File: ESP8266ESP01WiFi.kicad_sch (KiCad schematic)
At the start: 5 parts, among them IC1 TXS0104ED, J1 M20-7830446, U1 ESP-01v090

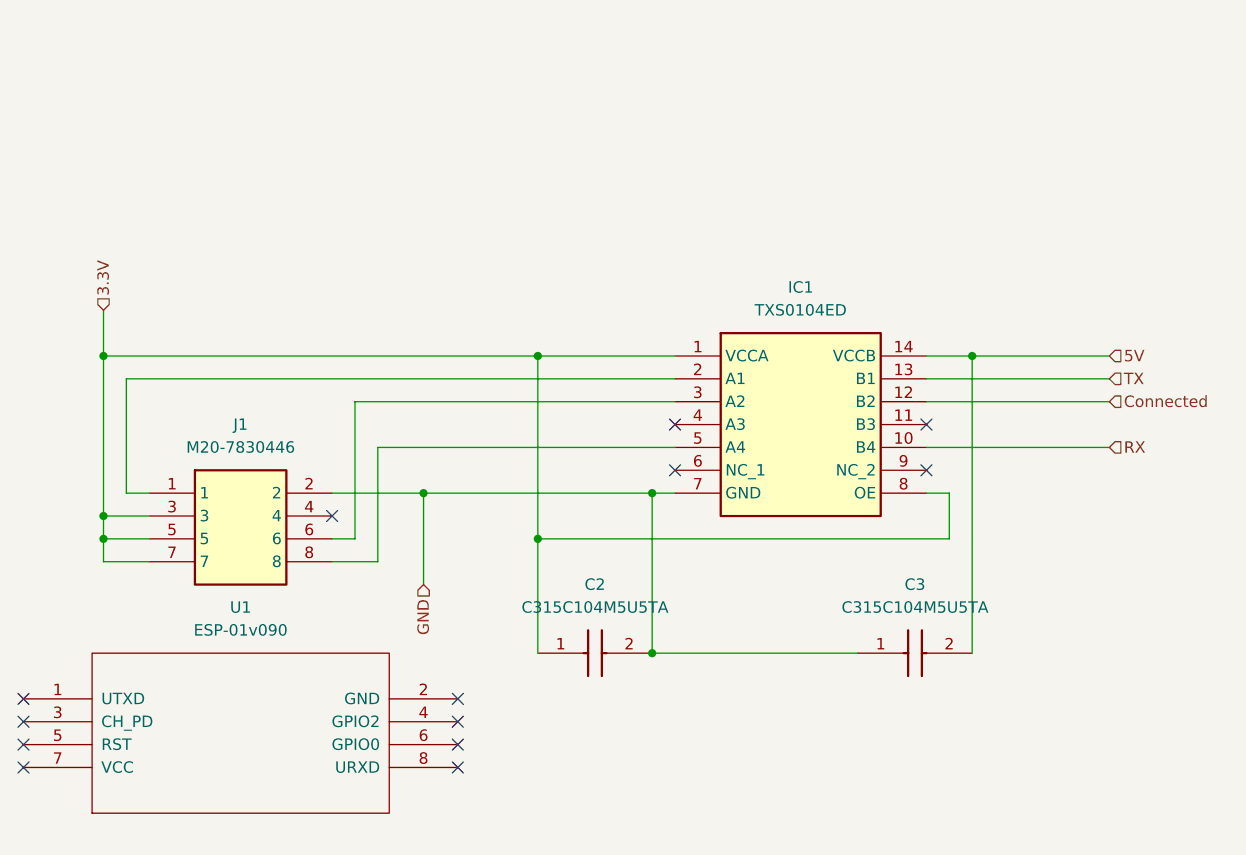
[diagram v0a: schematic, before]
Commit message: Swapped components for those in custom library, updated labelling on PCB.
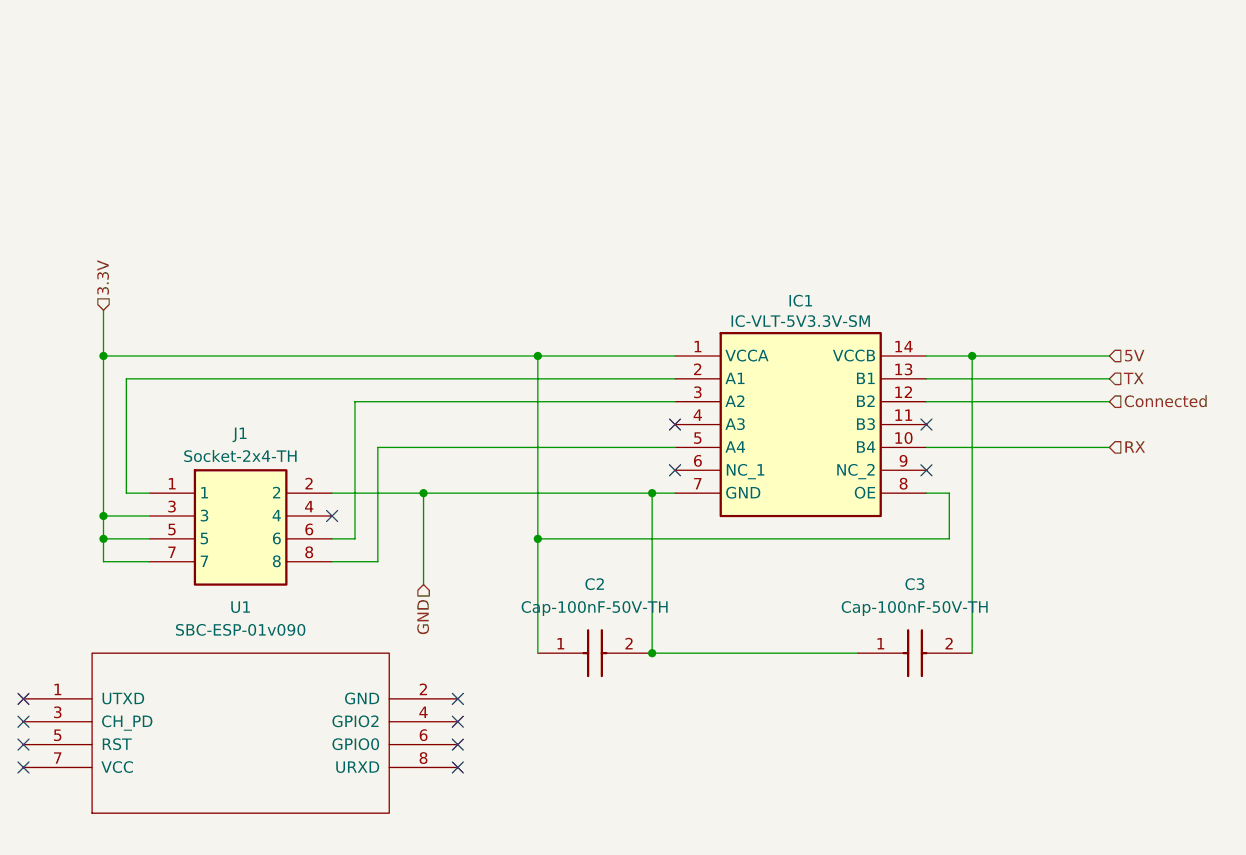
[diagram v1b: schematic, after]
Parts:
- C2, C3: value C315C104M5U5TA -> Cap-100nF-50V-TH; footprint SamacSys_Parts:C315C100J2G5TA -> Custom:80-C315C104M5U; symbol SamacSys_Parts:C315C104M5U5TA -> Custom:Cap-100nF-50V-TH; Supplier (none) -> Mouser; Supplier Part Number (none) -> 80-C315C104M5U; Supplier Price/Stock (none) -> https://www.mouser.co.uk/ProductDetail/KEMET/C315C104M5U5TA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
- IC1: value TXS0104ED -> IC-VLT-5V3.3V-SM; footprint SamacSys_Parts:SOIC127P600X175-14N -> Custom:595-TXS0104ED; symbol SamacSys_Parts:TXS0104ED -> Custom:IC-VLT-5V3.3V-SM; Supplier (none) -> Mouser; Supplier Part Number (none) -> 595-TXS0104ED; Supplier Price/Stock (none) -> https://www.mouser.co.uk/ProductDetail/Texas-Instruments/TX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
- J1: value M20-7830446 -> Socket-2x4-TH; footprint SamacSys_Parts:RHDR8W70P254X254_2X4_1056X500X850P -> Custom:855-M20-7830446; symbol SamacSys_Parts:M20-7830446 -> Custom:Socket-2x4-TH; Supplier (none) -> Mouser; Supplier Part Number (none) -> 855-M20-7830446; Supplier Price/Stock (none) -> https://www.mouser.co.uk/ProductDetail/Harwin/M20-7830446?q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
- U1: value ESP-01v090 -> SBC-ESP-01v090; footprint ESP8266:ESP-01 -> Custom:SBC-ESP8266ESP-01; symbol ESP8266:ESP-01v090 -> Custom:SBC-ESP-01v090
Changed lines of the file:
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@@
 	)
 	(symbol
-		(lib_id "SamacSys_Parts:M20-7830446")
+		(lib_id "Custom:Socket-2x4-TH")
 		(at 83.82 83.82 0)
 		(unit 1)
@@
 		(on_board yes)
 		(dnp no)
-		(fields_autoplaced yes)
 		(property "Reference" "J1"
-			(at 93.98 76.2 0)
-			(effects
-				(font
-					(size 1.27 1.27)
-				)
-			)
-		)
-		(property "Value" "M20-7830446"
-			(at 93.98 78.74 0)
-			(effects
-				(font
-					(size 1.27 1.27)
-				)
-			)
-		)
-		(property "Footprint" "SamacSys_Parts:RHDR8W70P254X254_2X4_1056X500X850P"
+			(at 93.98 77.216 0)
+			(effects
+				(font
+					(size 1.27 1.27)
+				)
+			)
+		)
+		(property "Value" "Socket-2x4-TH"
+			(at 93.98 79.756 0)
+			(effects
+				(font
+					(size 1.27 1.27)
+				)
+			)
+		)
+		(property "Footprint" "Custom:855-M20-7830446"
 			(at 100.33 178.74 0)
 			(effects
@@
 		(property "Manufacturer_Part_Number" "M20-7830446"
 			(at 100.33 878.74 0)
+			(effects
+				(font
+					(size 1.27 1.27)
+				)
+				(justify left top)
+				(hide yes)
+			)
+		)
+		(property "Supplier" "Mouser"
+			(at 83.82 83.82 0)
+			(effects
+				(font
+					(size 1.27 1.27)
+				)
+				(hide yes)
+			)
+		)
+		(property "Supplier Part Number" "855-M20-7830446"
+			(at 100.33 578.74 0)
+			(effects
+				(font
+					(size 1.27 1.27)
+				)
+				(justify left top)
+				(hide yes)
+			)
+		)
+		(property "Supplier Price/Stock" "https://www.mouser.co.uk/ProductDetail/Harwin/M20-7830446?qs=vF78I%252BjhbY%2FEi6Q%2F1EBREA%3D%3D"
+			(at 100.33 678.74 0)
 			(effects
 				(font
@@
 	)
 	(symbol
-		(lib_id "SamacSys_Parts:TXS0104ED")
+		(lib_id "Custom:IC-VLT-5V3.3V-SM")
 		(at 142.24 68.58 0)
 		(unit 1)
@@
 		(dnp no)
 		(property "Reference" "IC1"
-			(at 156.21 60.96 0)
-			(effects
-				(font
-					(size 1.27 1.27)
-				)
-			)
-		)
-		(property "Value" "TXS0104ED"
-			(at 156.21 63.5 0)
-			(effects
-				(font
-					(size 1.27 1.27)
-				)
-			)
-		)
-		(property "Footprint" "SamacSys_Parts:SOIC127P600X175-14N"
+			(at 156.21 62.484 0)
+			(effects
+				(font
+					(size 1.27 1.27)
+				)
+			)
+		)
+		(property "Value" "IC-VLT-5V3.3V-SM"
+			(at 156.21 64.008 0)
+			(effects
+				(font
+					(size 1.27 1.27)
+				)
+				(justify top)
+			)
+		)
+		(property "Footprint" "Custom:595-TXS0104ED"
 			(at 166.37 163.5 0)
 			(effects
@@
 			)
 		)
-		(property "Description" "TXS0104ED, Voltage Level Translator, Open Drain 1.65 to 3.6, 2.3 to 5.5V 14-Pin SOIC"
+		(property "Description" "IC - TXS0104ED, Voltage Level Translator, Open Drain 1.65 to 3.6, 2.3 to 5.5V 14-Pin SOIC"
 			(at 142.24 68.58 0)
 			(effects
@@
 		(property "Manufacturer_Part_Number" "TXS0104ED"
 			(at 166.37 863.5 0)
+			(effects
+				(font
+					(size 1.27 1.27)
+				)
+				(justify left top)
+				(hide yes)
+			)
+		)
+		(property "Supplier" "Mouser"
+			(at 142.24 68.58 0)
+			(effects
+				(font
+					(size 1.27 1.27)
+				)
+				(hide yes)
+			)
+		)
+		(property "Supplier Part Number" "595-TXS0104ED"
+			(at 166.37 563.5 0)
+			(effects
+				(font
+					(size 1.27 1.27)
+				)
+				(justify left top)
+				(hide yes)
+			)
+		)
+		(property "Supplier Price/Stock" "https://www.mouser.co.uk/ProductDetail/Texas-Instruments/TXS0104ED?qs=7kv20MEVUlg5V59AplM5UA%3D%3D"
+			(at 166.37 663.5 0)
 			(effects
 				(font
@@
 	)
 	(symbol
-		(lib_id "ESP8266:ESP-01v090")
+		(lib_id "Custom:SBC-ESP-01v090")
 		(at 93.98 110.49 0)
 		(unit 1)
@@
 			)
 		)
-		(property "Value" "ESP-01v090"
+		(property "Value" "SBC-ESP-01v090"
 			(at 93.98 99.06 0)
 			(effects
@@
 			)
 		)
-		(property "Footprint" "ESP8266:ESP-01"
+		(property "Footprint" "Custom:SBC-ESP8266ESP-01"
 			(at 93.98 110.49 0)
 			(effects
@@
 	)
 	(symbol
-		(lib_id "SamacSys_Parts:C315C104M5U5TA")
+		(lib_id "Custom:Cap-100nF-50V-TH")
 		(at 162.56 101.6 0)
 		(unit 1)
@@
 			)
 		)
-		(property "Value" "C315C104M5U5TA"
+		(property "Value" "Cap-100nF-50V-TH"
 			(at 168.91 96.52 0)
 			(effects
@@
 			)
 		)
-		(property "Footprint" "SamacSys_Parts:C315C100J2G5TA"
+		(property "Footprint" "Custom:80-C315C104M5U"
 			(at 171.45 197.79 0)
 			(effects
@@
 		(property "Manufacturer_Part_Number" "C315C104M5U5TA"
 			(at 171.45 897.79 0)
+			(effects
+				(font
+					(size 1.27 1.27)
+				)
+				(justify left top)
+				(hide yes)
+			)
+		)
+		(property "Supplier" "Mouser"
+			(at 162.56 101.6 0)
+			(effects
+				(font
+					(size 1.27 1.27)
+				)
+				(hide yes)
+			)
+		)
+		(property "Supplier Part Number" "80-C315C104M5U"
+			(at 171.45 597.79 0)
+			(effects
+				(font
+					(size 1.27 1.27)
+				)
+				(justify left top)
+				(hide yes)
+			)
+		)
+		(property "Supplier Price/Stock" "https://www.mouser.co.uk/ProductDetail/KEMET/C315C104M5U5TA?qs=yPUL72EuMSdlpklLgkTxlg%3D%3D"
+			(at 171.45 697.79 0)
 			(effects
 				(font
@@
 	)
 	(symbol
-		(lib_name "C315C104M5U5TA_1")
-		(lib_id "SamacSys_Parts:C315C104M5U5TA")
+		(lib_id "Custom:Cap-100nF-50V-TH")
 		(at 127 101.6 0)
 		(unit 1)
@@
 			)
 		)
-		(property "Value" "C315C104M5U5TA"
+		(property "Value" "Cap-100nF-50V-TH"
 			(at 133.35 96.52 0)
 			(effects
@@
 			)
 		)
-		(property "Footprint" "SamacSys_Parts:C315C100J2G5TA"
+		(property "Footprint" "Custom:80-C315C104M5U"
 			(at 135.89 197.79 0)
 			(effects
@@
 			(effects
 				(font
+					(size 1.27 1.27)
+				)
+				(justify left top)
+				(hide yes)
+			)
+		)
+		(property "Supplier" "Mouser"
+			(at 127 101.6 0)
+			(effects
+				(font
+					(size 1.27 1.27)
+				)
+				(hide yes)
+			)
+		)
+		(property "Supplier Part Number" "80-C315C104M5U"
+			(at 135.89 597.79 0)
+			(effects
+				(font
+					(size 1.27 1.27)
+				)
+				(justify left top)
+				(hide yes)
+			)
+		)
+		(property "Supplier Price/Stock" "https://www.mouser.co.uk/ProductDetail/KEMET/C315C104M5U5TA?qs=yPUL72EuMSdlpklLgkTxlg%3D%3D"
+			(at 135.89 697.79 0)
+			(effects
+				(font

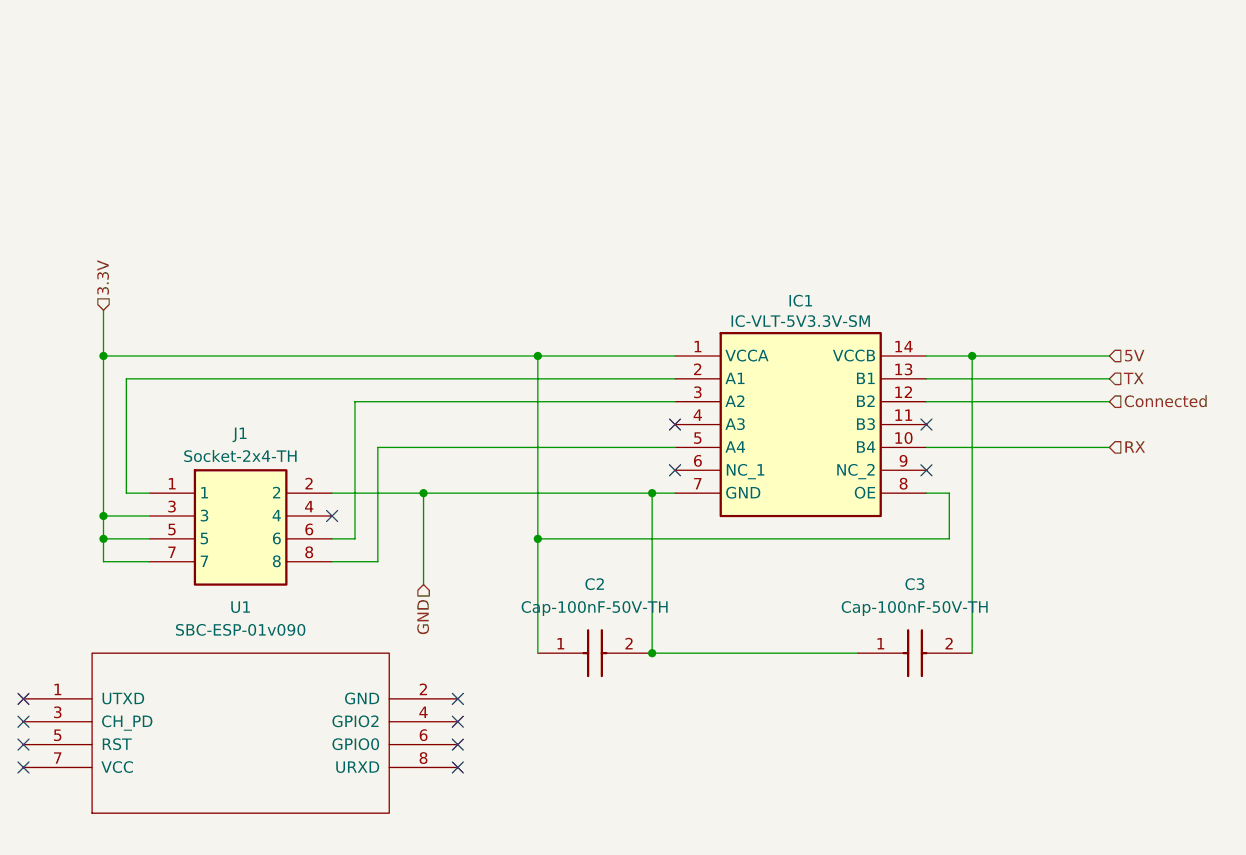
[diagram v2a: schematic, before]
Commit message: Added appropriate logic level shifter based on 2N7000 design.
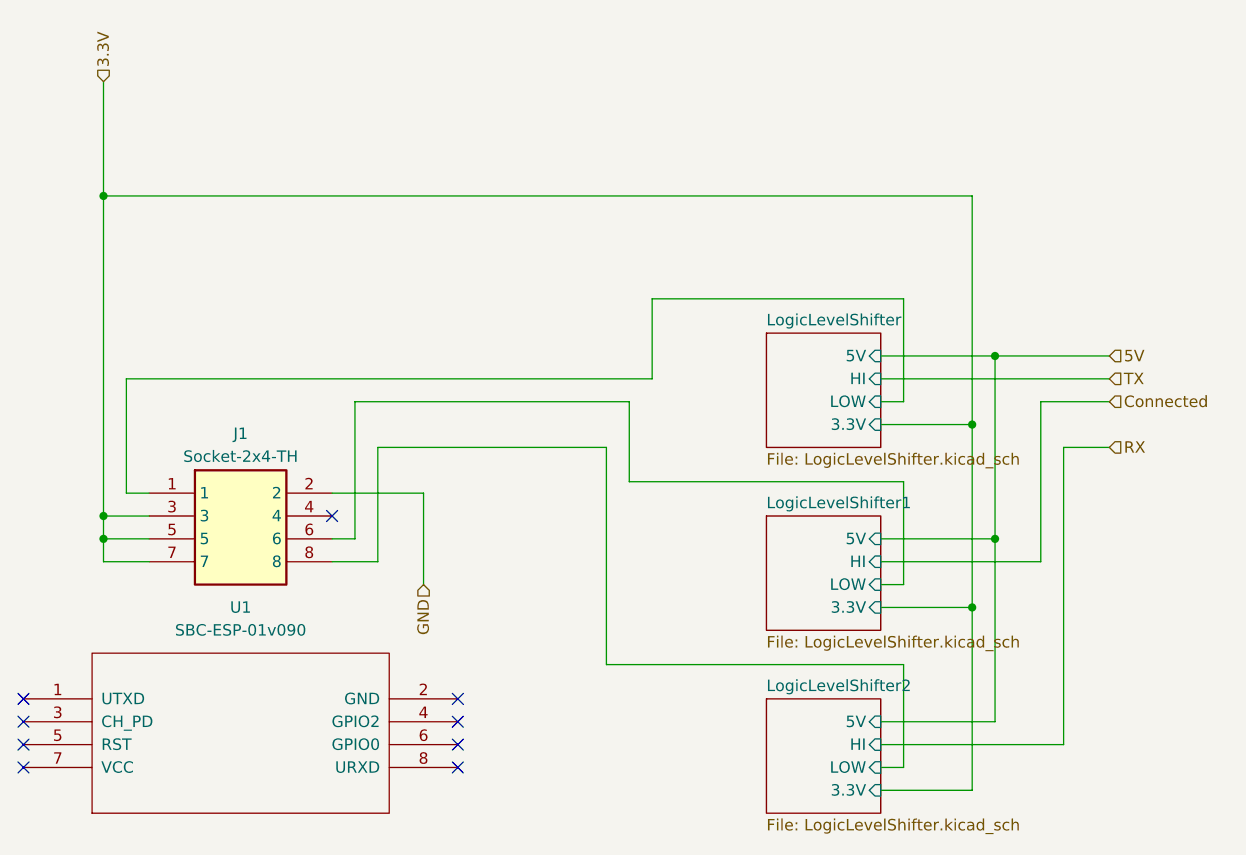
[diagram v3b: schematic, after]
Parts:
- removed C2, C3: Cap-100nF-50V-TH, Custom:80-C315C104M5U, symbol Custom:Cap-100nF-50V-TH
- removed IC1: IC-VLT-5V3.3V-SM, Custom:595-TXS0104ED, symbol Custom:IC-VLT-5V3.3V-SM
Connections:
- net LogicLevelShifter/LOW: now reaches J1.1
- net LogicLevelShifter1/LOW: now reaches J1.6
- net LogicLevelShifter2/LOW: now reaches J1.8
- no-connect marks 13 -> 9
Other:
- added sheet LogicLevelShifter (LogicLevelShifter.kicad_sch)
- added sheet LogicLevelShifter1 (LogicLevelShifter.kicad_sch)
- added sheet LogicLevelShifter2 (LogicLevelShifter.kicad_sch)

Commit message: Updates look good, promoted to v1.2.
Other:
- title: ESP8266 ESP-01 WiFi Module -> Arduino Mega CMRI WiFi Shield
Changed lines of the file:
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@@
 	(paper "A4")
 	(title_block
-		(title "ESP8266 ESP-01 WiFi Module")
-		(date "2026-01-30")
-		(rev "1.1")
+		(title "Arduino Mega CMRI WiFi Shield")
+		(date "2026-02-10")
+		(rev "1.2")
 	)
 	(junction
